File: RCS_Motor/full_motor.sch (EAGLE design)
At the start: 13 parts, among them IC1 ILD213T, M1 SMALL_SERVO, T1 2N2222

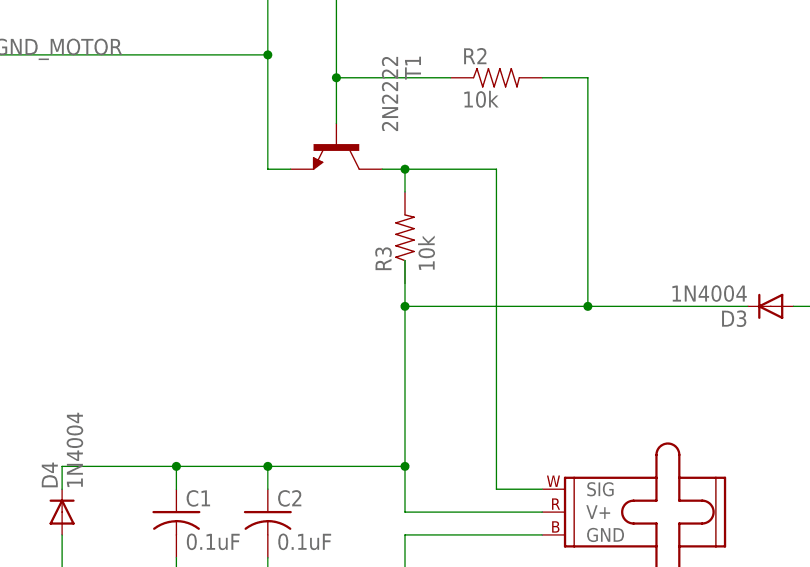
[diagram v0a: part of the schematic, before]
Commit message: Fixed connection with resistor
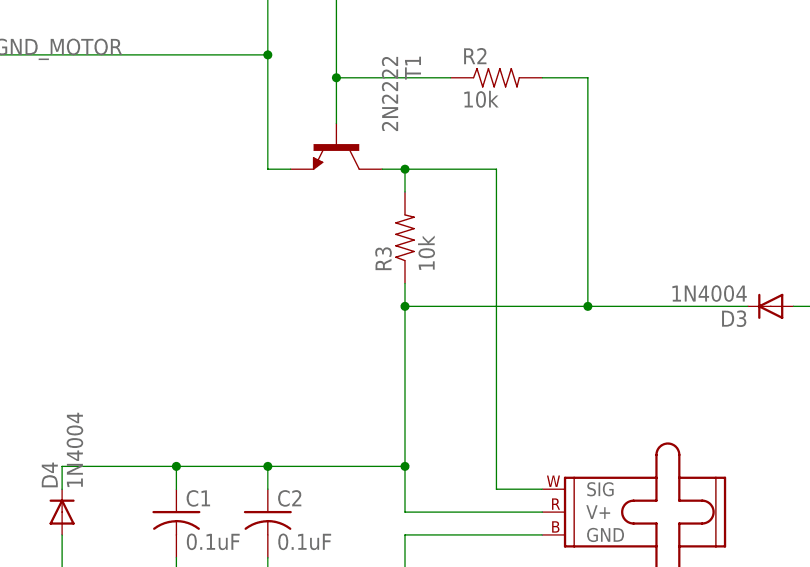
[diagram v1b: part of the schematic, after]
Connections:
- net N$2: now also R3.1
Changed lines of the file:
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@@
 <wire x1="96.52" y1="99.06" x2="96.52" y2="73.66" width="0.1524" layer="91"/>
 <wire x1="96.52" y1="73.66" x2="76.2" y2="73.66" width="0.1524" layer="91"/>
-<junction x="76.2" y="73.66"/>
-<wire x1="76.2" y1="78.74" x2="76.2" y2="73.66" width="0.1524" layer="91"/>
 <pinref part="D3" gate="1" pin="C"/>
 <wire x1="96.52" y1="73.66" x2="114.3" y2="73.66" width="0.1524" layer="91"/>
 <junction x="96.52" y="73.66"/>
+<pinref part="R3" gate="G$1" pin="1"/>
+<wire x1="76.2" y1="76.2" x2="76.2" y2="73.66" width="0.1524" layer="91"/>
+<junction x="76.2" y="73.66"/>
 </segment>
 </net>

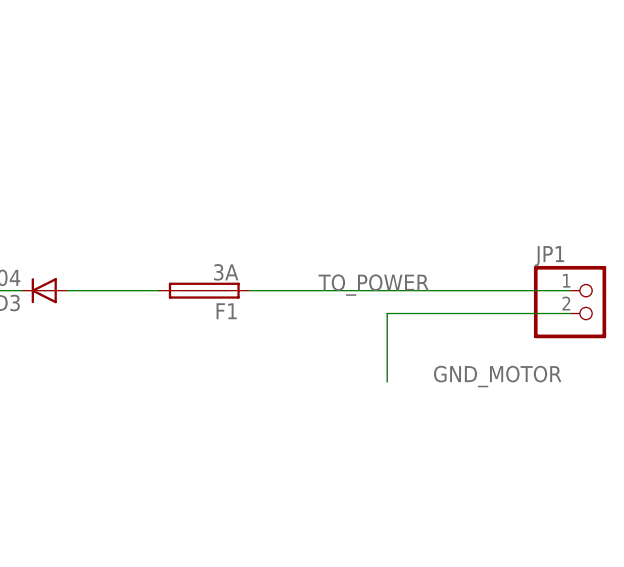
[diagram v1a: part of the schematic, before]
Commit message: Added label to power and fixed resistor connection
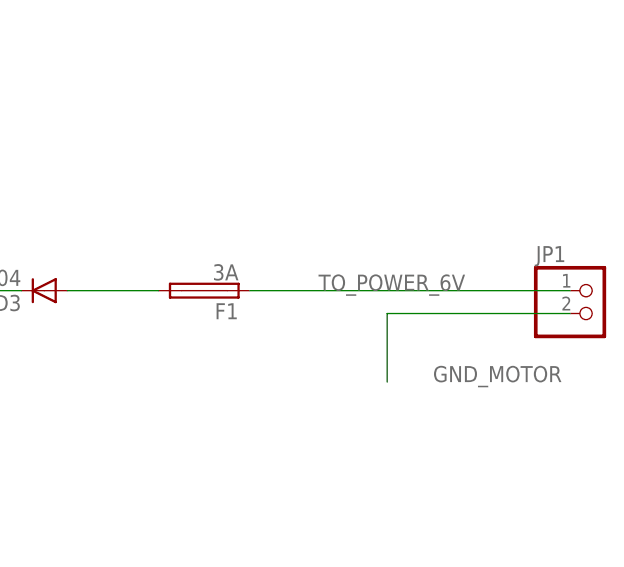
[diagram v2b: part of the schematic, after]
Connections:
- net TO_POWER renamed TO_POWER_6V
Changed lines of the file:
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@@
 </segment>
 </net>
-<net name="TO_POWER" class="0">
+<net name="TO_POWER_6V" class="0">
 <segment>
 <pinref part="F1" gate="1" pin="1"/>
